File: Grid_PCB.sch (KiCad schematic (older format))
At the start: 1 part, among them U1 74LS151

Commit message: transered nested project into root and moved docs into docs/ folder
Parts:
- removed U1: 74LS151, symbol 74xx:74LS151
- added J10: LED_Conn, Connector_PinHeader_2.54mm:PinHeader_1x02_P2.54mm_Horizontal, symbol Connector:Conn_01x02_Male
- added J9: ESP_Conn, Connector_PinHeader_2.54mm:PinHeader_1x08_P2.54mm_Horizontal, symbol grid:ESP_Conn
- added U1: SN74HC151N, Package_DIP:DIP-16_W7.62mm, symbol grid:SN74HC151N
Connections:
- net labels added: BTN1, BTN2, BTN3, BTN4, BTN5, BTN6, BTN7, ESPselA, ESPselB, ESPselC, LED_In, LED_Link, LED_Out, MUX_OUT
- net labels removed: LED_Serial
- wire segments 4 -> 43
- no-connect marks 0 -> 2
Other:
- note added: "Note the order of these can be changed for ease of routing\njust needs to match up with esp connector (or not, we could just change\norientations/ordering in the cables)"
- note added: "TODO: DO WE WANT TO CONNECT STROBE TO TEST PAD FOR DEBUGGING?"
- note added: "Y = output\nW = inverted output\nG = inverted strobe"
- note removed: "NOTE: we are using the 74HC151 \n(from the shop) but this has \nidentical pinout"

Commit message: temp
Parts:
- U1: footprint Package_DIP:DIP-16_W7.62mm -> Battery:BatteryHolder_Keystone_3000_1x12mm
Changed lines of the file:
@@
 F 0 "U1" H 3250 5225 50  0000 C CNN
 F 1 "SN74HC151N" H 3250 5134 50  0000 C CNN
-F 2 "Package_DIP:DIP-16_W7.62mm" H 3300 4650 50  0001 C CNN
+F 2 "Battery:BatteryHolder_Keystone_3000_1x12mm" H 3300 4650 50  0001 C CNN
 F 3 "https://www.ti.com/lit/ds/symlink/sn74hc151.pdf?ts=1632846774937&ref_url=https%253A%252F%252Fwww.google.com%252F" H 3300 4650 50  0001 C CNN
 	1    3250 4650

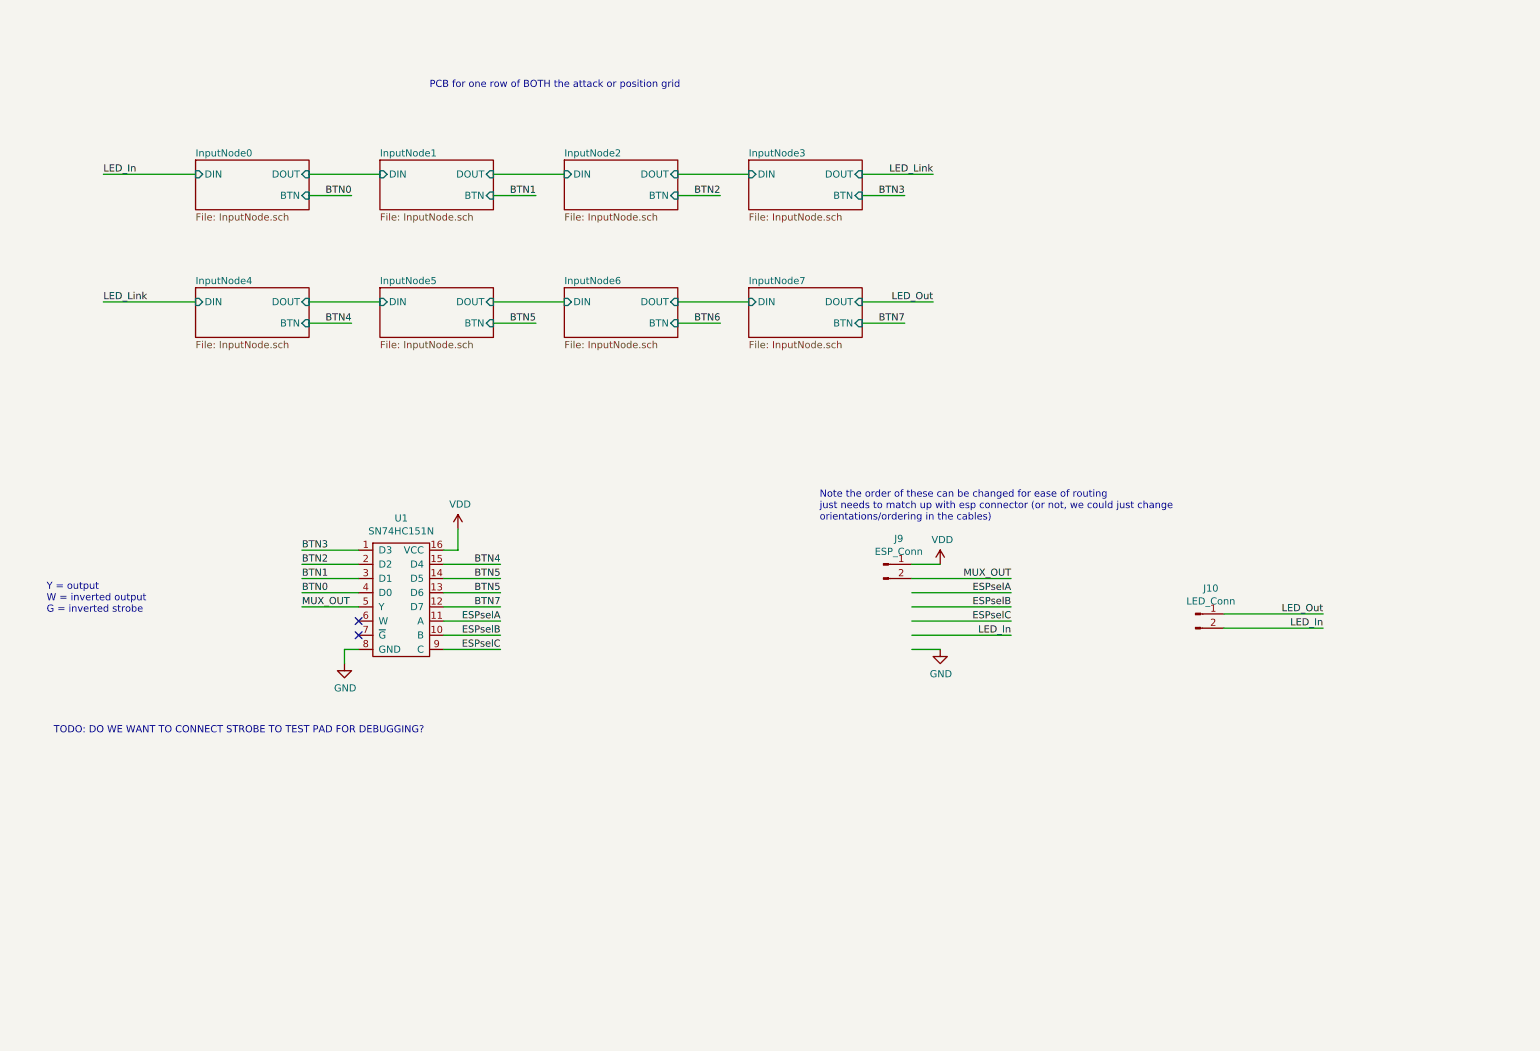
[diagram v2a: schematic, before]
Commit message: updated for homepage
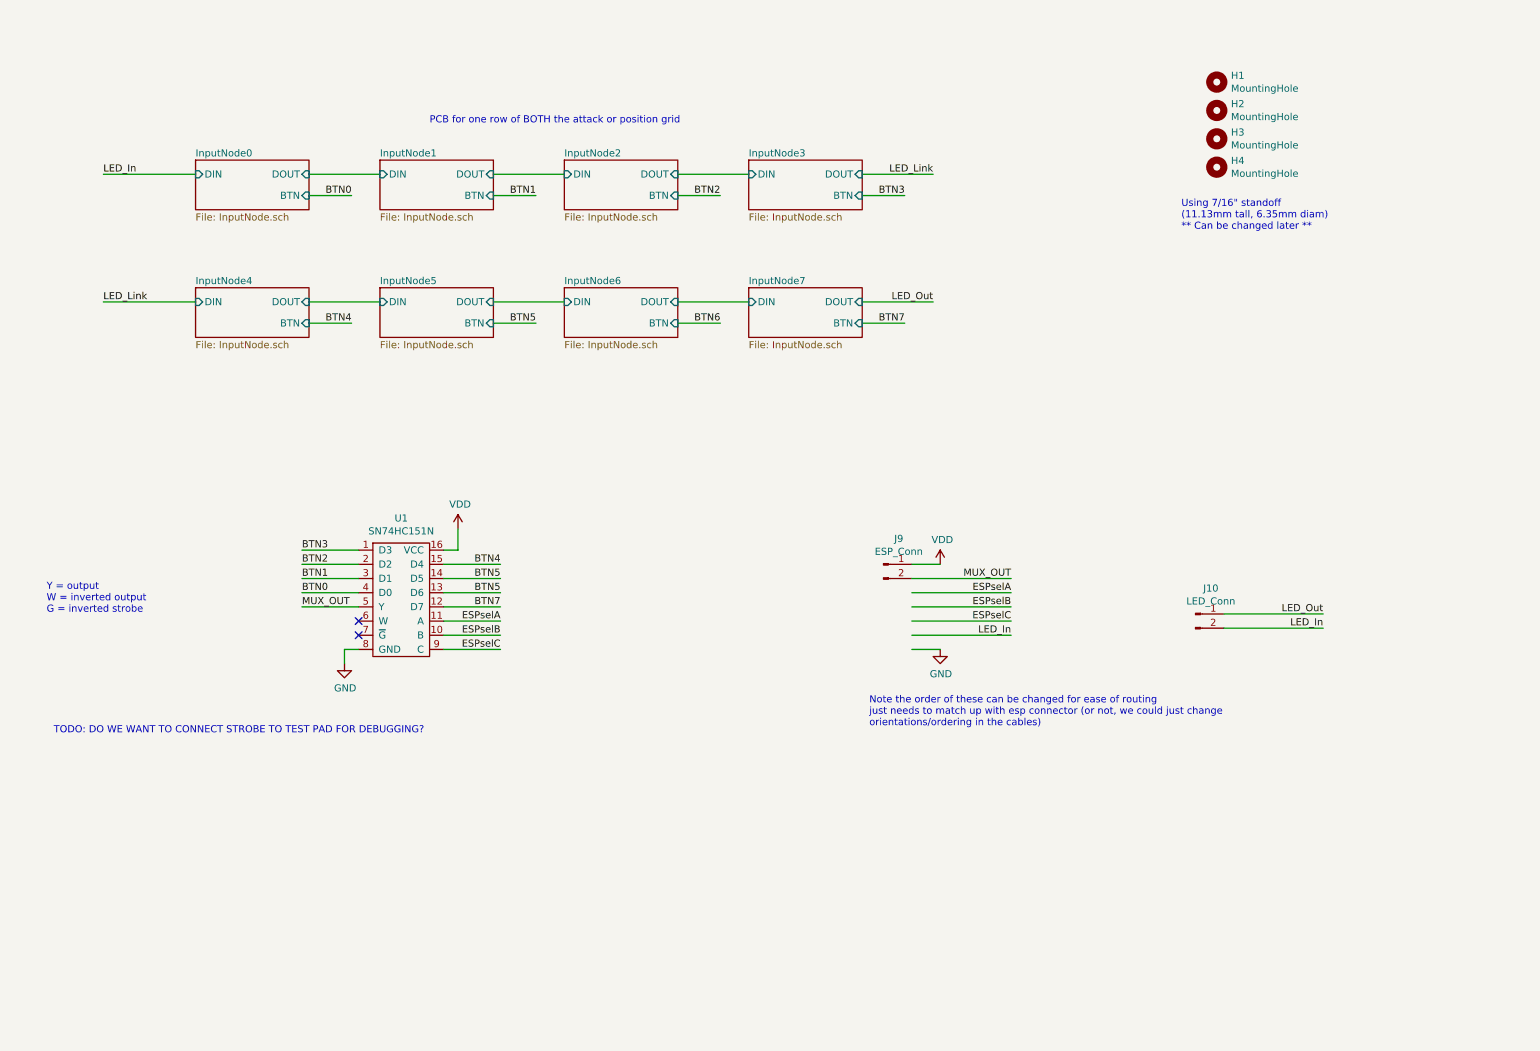
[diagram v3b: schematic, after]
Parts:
- added H1, H2, H3, H4: MountingHole, MountingHole:MountingHole_6.4mm_M6, symbol Mechanical:MountingHole
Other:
- note added: "Using 7/16" standoff \n(11.13mm tall, 6.35mm diam)\n** Can be changed later **"
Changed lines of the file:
@@
 Text Label 6800 2700 2    50   ~ 0
 BTN7
-Text Notes 3450 1050 0    50   ~ 0
+Text Notes 3450 1300 0    50   ~ 0
 PCB for one row of BOTH the attack or position grid
 Wire Wire Line
@@
 Text Label 7550 4500 2    50   ~ 0
 MUX_OUT
-Text Notes 6200 4100 0    50   ~ 0
+Text Notes 6550 5550 0    50   ~ 0
 Note the order of these can be changed for ease of routing\njust needs to match up with esp connector (or not, we could just change\norientations/ordering in the cables)
 Text Label 7550 4600 2    50   ~ 0
@@
 	1    0    0    -1
 $EndComp
+$Comp
+L Mechanical:MountingHole H1
+U 1 1 61A94890
+P 9000 1000
+F 0 "H1" H 9100 1046 50  0000 L CNN
+F 1 "MountingHole" H 9100 955 50  0000 L CNN
+F 2 "MountingHole:MountingHole_6.4mm_M6" H 9000 1000 50  0001 C CNN
+F 3 "~" H 9000 1000 50  0001 C CNN
+	1    9000 1000
+	1    0    0    -1
+$EndComp
+$Comp
+L Mechanical:MountingHole H2
+U 1 1 61A94CB6
+P 9000 1200
+F 0 "H2" H 9100 1246 50  0000 L CNN
+F 1 "MountingHole" H 9100 1155 50  0000 L CNN
+F 2 "MountingHole:MountingHole_6.4mm_M6" H 9000 1200 50  0001 C CNN
+F 3 "~" H 9000 1200 50  0001 C CNN
+	1    9000 1200
+	1    0    0    -1
+$EndComp
+$Comp
+L Mechanical:MountingHole H3
+U 1 1 61A94DFE
+P 9000 1400
+F 0 "H3" H 9100 1446 50  0000 L CNN
+F 1 "MountingHole" H 9100 1355 50  0000 L CNN
+F 2 "MountingHole:MountingHole_6.4mm_M6" H 9000 1400 50  0001 C CNN
+F 3 "~" H 9000 1400 50  0001 C CNN
+	1    9000 1400
+	1    0    0    -1
+$EndComp
+$Comp
+L Mechanical:MountingHole H4
+U 1 1 61A94FF8
+P 9000 1600
+F 0 "H4" H 9100 1646 50  0000 L CNN
+F 1 "MountingHole" H 9100 1555 50  0000 L CNN
+F 2 "MountingHole:MountingHole_6.4mm_M6" H 9000 1600 50  0001 C CNN
+F 3 "~" H 9000 1600 50  0001 C CNN
+	1    9000 1600
+	1    0    0    -1
+$EndComp
+Text Notes 8750 2050 0    50   ~ 0
+Using 7/16" standoff \n(11.13mm tall, 6.35mm diam)\n** Can be changed later **
 $EndSCHEMATC

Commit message: added resistor network and updated mnt hole footprint
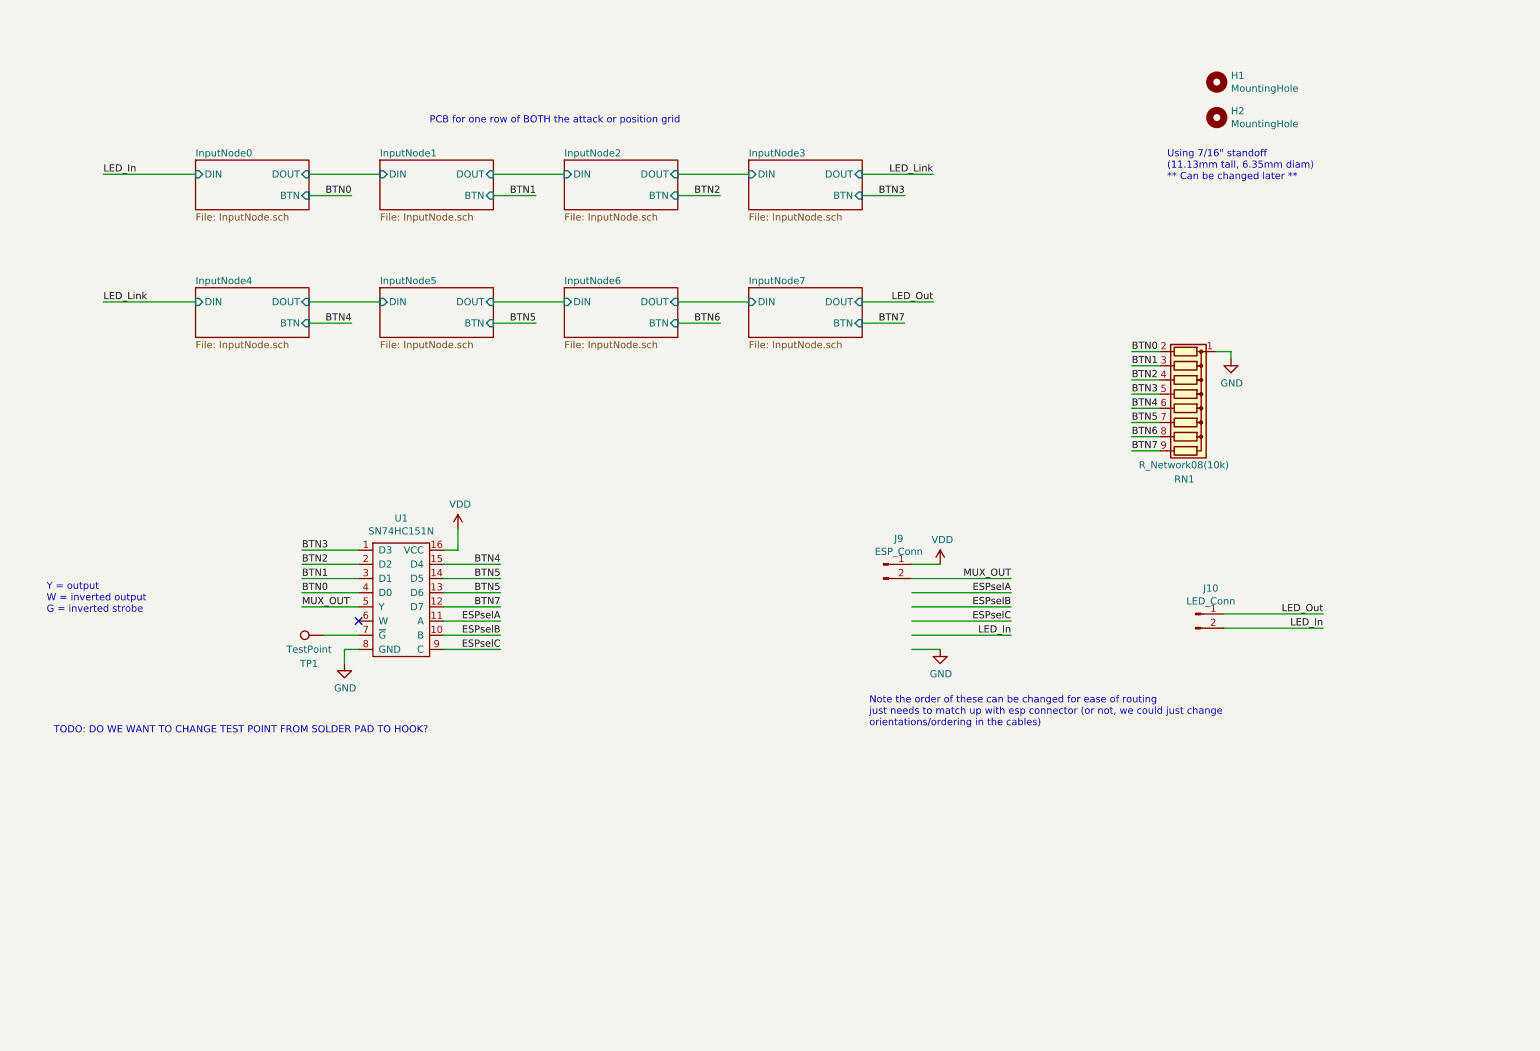
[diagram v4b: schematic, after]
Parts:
- removed H3, H4: MountingHole, MountingHole:MountingHole_6.4mm_M6, symbol Mechanical:MountingHole
- added RN1: R_Network08(10k), Resistor_THT:R_Array_SIP9, symbol Device:R_Network08
- added TP1: TestPoint, TestPoint:TestPoint_Pad_2.5x2.5mm, symbol Connector:TestPoint
- H1, H2: footprint MountingHole:MountingHole_6.4mm_M6 -> MountingHole:MountingHole_3.2mm_M3
- U1: footprint Battery:BatteryHolder_Keystone_3000_1x12mm -> Package_DIP:DIP-16_W10.16mm
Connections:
- wire segments 43 -> 54
- no-connect marks 2 -> 1
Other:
- note added: "TODO: DO WE WANT TO CHANGE TEST POINT FROM SOLDER PAD TO HOOK?"
- note removed: "TODO: DO WE WANT TO CONNECT STROBE TO TEST PAD FOR DEBUGGING?"
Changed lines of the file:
@@
 F 0 "U1" H 3250 5225 50  0000 C CNN
 F 1 "SN74HC151N" H 3250 5134 50  0000 C CNN
-F 2 "Battery:BatteryHolder_Keystone_3000_1x12mm" H 3300 4650 50  0001 C CNN
+F 2 "Package_DIP:DIP-16_W10.16mm" H 3300 4650 50  0001 C CNN
 F 3 "https://www.ti.com/lit/ds/symlink/sn74hc151.pdf?ts=1632846774937&ref_url=https%253A%252F%252Fwww.google.com%252F" H 3300 4650 50  0001 C CNN
 	1    3250 4650
@@
 Wire Wire Line
 	6850 4500 7550 4500
-NoConn ~ 2950 4900
 Text Notes 800  5600 0    50   ~ 0
-TODO: DO WE WANT TO CONNECT STROBE TO TEST PAD FOR DEBUGGING?
+TODO: DO WE WANT TO CHANGE TEST POINT FROM SOLDER PAD TO HOOK?
 NoConn ~ 2950 4800
 Text Label 2550 4700 0    50   ~ 0
@@
 F 0 "H1" H 9100 1046 50  0000 L CNN
 F 1 "MountingHole" H 9100 955 50  0000 L CNN
-F 2 "MountingHole:MountingHole_6.4mm_M6" H 9000 1000 50  0001 C CNN
-F 3 "~" H 9000 1000 50  0001 C CNN
+F 2 "MountingHole:MountingHole_3.2mm_M3" H 9000 1000 50  0001 C CNN
+F 3 "https://www.digikey.com/en/products/detail/essentra-components/50M030050F012/11639328~" H 9000 1000 50  0001 C CNN
 	1    9000 1000
 	1    0    0    -1
 $EndComp
+Text Notes 8650 1700 0    50   ~ 0
+Using 7/16" standoff \n(11.13mm tall, 6.35mm diam)\n** Can be changed later **
+$Comp
+L Connector:TestPoint TP1
+U 1 1 615B44CF
+P 2700 4900
+F 0 "TP1" V 2500 5000 50  0000 C CNN
+F 1 "TestPoint" V 2600 5000 50  0000 C CNN
+F 2 "TestPoint:TestPoint_Pad_2.5x2.5mm" H 2900 4900 50  0001 C CNN
+F 3 "~" H 2900 4900 50  0001 C CNN
+	1    2700 4900
+	0    -1   -1   0
+$EndComp
+Wire Wire Line
+	2700 4900 2950 4900
+$Comp
+L Device:R_Network08 RN1
+U 1 1 615B83C9
+P 8800 3300
+F 0 "RN1" V 9300 3200 50  0000 L CNN
+F 1 "R_Network08(10k)" V 9200 2950 50  0000 L CNN
+F 2 "Resistor_THT:R_Array_SIP9" V 9275 3300 50  0001 C CNN
+F 3 "http://www.vishay.com/docs/31509/csc.pdf" H 8800 3300 50  0001 C CNN
+	1    8800 3300
+	0    1    1    0
+$EndComp
+$Comp
+L power:GND #PWR051
+U 1 1 615BC30E
+P 9100 2950
+F 0 "#PWR051" H 9100 2700 50  0001 C CNN
+F 1 "GND" H 9105 2777 50  0000 C CNN
+F 2 "" H 9100 2950 50  0001 C CNN
+F 3 "" H 9100 2950 50  0001 C CNN
+	1    9100 2950
+	1    0    0    -1
+$EndComp
+Text Label 8400 2900 0    50   ~ 0
+BTN0
+Wire Wire Line
+	8400 2900 8600 2900
+Text Label 8400 3000 0    50   ~ 0
+BTN1
+Wire Wire Line
+	8400 3000 8600 3000
+Text Label 8400 3100 0    50   ~ 0
+BTN2
+Wire Wire Line
+	8400 3100 8600 3100
+Text Label 8400 3200 0    50   ~ 0
+BTN3
+Wire Wire Line
+	8400 3200 8600 3200
+Text Label 8400 3300 0    50   ~ 0
+BTN4
+Wire Wire Line
+	8400 3300 8600 3300
+Text Label 8400 3400 0    50   ~ 0
+BTN5
+Wire Wire Line
+	8400 3400 8600 3400
+Text Label 8400 3500 0    50   ~ 0
+BTN6
+Wire Wire Line
+	8400 3500 8600 3500
+Text Label 8400 3600 0    50   ~ 0
+BTN7
+Wire Wire Line
+	8400 3600 8600 3600
+Wire Wire Line
+	9000 2900 9100 2900
+Wire Wire Line
+	9100 2900 9100 2950
 $Comp
 L Mechanical:MountingHole H2
-U 1 1 61A94CB6
-P 9000 1200
-F 0 "H2" H 9100 1246 50  0000 L CNN
-F 1 "MountingHole" H 9100 1155 50  0000 L CNN
-F 2 "MountingHole:MountingHole_6.4mm_M6" H 9000 1200 50  0001 C CNN
-F 3 "~" H 9000 1200 50  0001 C CNN
-	1    9000 1200
-	1    0    0    -1
-$EndComp
-$Comp
-L Mechanical:MountingHole H3
-U 1 1 61A94DFE
-P 9000 1400
-F 0 "H3" H 9100 1446 50  0000 L CNN
-F 1 "MountingHole" H 9100 1355 50  0000 L CNN
-F 2 "MountingHole:MountingHole_6.4mm_M6" H 9000 1400 50  0001 C CNN
-F 3 "~" H 9000 1400 50  0001 C CNN
-	1    9000 1400
-	1    0    0    -1
-$EndComp
-$Comp
-L Mechanical:MountingHole H4
-U 1 1 61A94FF8
-P 9000 1600
-F 0 "H4" H 9100 1646 50  0000 L CNN
-F 1 "MountingHole" H 9100 1555 50  0000 L CNN
-F 2 "MountingHole:MountingHole_6.4mm_M6" H 9000 1600 50  0001 C CNN
-F 3 "~" H 9000 1600 50  0001 C CNN
-	1    9000 1600
-	1    0    0    -1
-$EndComp
-Text Notes 8750 2050 0    50   ~ 0
-Using 7/16" standoff \n(11.13mm tall, 6.35mm diam)\n** Can be changed later **
+U 1 1 615D2E17
+P 9000 1250
+F 0 "H2" H 9100 1296 50  0000 L CNN
+F 1 "MountingHole" H 9100 1205 50  0000 L CNN
+F 2 "MountingHole:MountingHole_3.2mm_M3" H 9000 1250 50  0001 C CNN
+F 3 "https://www.digikey.com/en/products/detail/essentra-components/50M030050F012/11639328~" H 9000 1250 50  0001 C CNN
+	1    9000 1250
+	1    0    0    -1
+$EndComp
 $EndSCHEMATC

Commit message: finished first pass at routing
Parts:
- removed RN1: R_Network08(10k), Resistor_THT:R_Array_SIP9, symbol Device:R_Network08
- added H3, H4: MountingHole, MountingHole:MountingHole_3.2mm_M3, symbol Mechanical:MountingHole
- J9: footprint Connector_PinHeader_2.54mm:PinHeader_1x08_P2.54mm_Horizontal -> Connector_PinHeader_2.54mm:PinHeader_1x07_P2.54mm_Horizontal
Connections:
- wire segments 54 -> 44
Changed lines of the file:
@@
 	3950 4500 3550 4500
 Text Label 3950 4600 2    50   ~ 0
-BTN5
+BTN6
 Wire Wire Line
 	3950 4600 3550 4600
@@
 PCB for one row of BOTH the attack or position grid
 Wire Wire Line
-	6850 4500 7550 4500
+	6850 4800 7550 4800
 Text Notes 800  5600 0    50   ~ 0
 TODO: DO WE WANT TO CHANGE TEST POINT FROM SOLDER PAD TO HOOK?
@@
 Wire Wire Line
 	2550 4700 2950 4700
-Text Label 7550 4500 2    50   ~ 0
+Text Label 7550 4800 2    50   ~ 0
 MUX_OUT
 Text Notes 6550 5550 0    50   ~ 0
 Note the order of these can be changed for ease of routing\njust needs to match up with esp connector (or not, we could just change\norientations/ordering in the cables)
+Text Label 7550 4700 2    50   ~ 0
+ESPselA
+Text Label 7550 4500 2    50   ~ 0
+ESPselC
 Text Label 7550 4600 2    50   ~ 0
-ESPselA
-Text Label 7550 4800 2    50   ~ 0
-ESPselC
-Text Label 7550 4700 2    50   ~ 0
 ESPselB
 Wire Wire Line
-	6850 4600 7550 4600
-Wire Wire Line
-	7550 4700 6850 4700
-Wire Wire Line
-	6850 4800 7550 4800
+	6850 4500 7550 4500
+Wire Wire Line
+	7550 4600 6850 4600
+Wire Wire Line
+	6850 4700 7550 4700
 Text Label 7550 4900 2    50   ~ 0
 LED_In
@@
 Wire Wire Line
 	9050 4750 9750 4750
+Text Label 9750 4750 2    50   ~ 0
+LED_In
+Wire Wire Line
+	9050 4850 9750 4850
 Text Label 9750 4850 2    50   ~ 0
-LED_In
-Wire Wire Line
-	9050 4850 9750 4850
-Text Label 9750 4750 2    50   ~ 0
 LED_Out
 Wire Wire Line
@@
 F 0 "J9" H 6758 5181 50  0000 C CNN
 F 1 "ESP_Conn" H 6758 5090 50  0000 C CNN
-F 2 "Connector_PinHeader_2.54mm:PinHeader_1x08_P2.54mm_Horizontal" H 6650 4700 50  0001 C CNN
+F 2 "Connector_PinHeader_2.54mm:PinHeader_1x07_P2.54mm_Horizontal" H 6650 4700 50  0001 C CNN
 F 3 "~" H 6650 4700 50  0001 C CNN
 	1    6650 4700
@@
 	2700 4900 2950 4900
 $Comp
-L Device:R_Network08 RN1
-U 1 1 615B83C9
-P 8800 3300
-F 0 "RN1" V 9300 3200 50  0000 L CNN
-F 1 "R_Network08(10k)" V 9200 2950 50  0000 L CNN
-F 2 "Resistor_THT:R_Array_SIP9" V 9275 3300 50  0001 C CNN
-F 3 "http://www.vishay.com/docs/31509/csc.pdf" H 8800 3300 50  0001 C CNN
-	1    8800 3300
-	0    1    1    0
-$EndComp
-$Comp
-L power:GND #PWR051
-U 1 1 615BC30E
-P 9100 2950
-F 0 "#PWR051" H 9100 2700 50  0001 C CNN
-F 1 "GND" H 9105 2777 50  0000 C CNN
-F 2 "" H 9100 2950 50  0001 C CNN
-F 3 "" H 9100 2950 50  0001 C CNN
-	1    9100 2950
-	1    0    0    -1
-$EndComp
-Text Label 8400 2900 0    50   ~ 0
-BTN0
-Wire Wire Line
-	8400 2900 8600 2900
-Text Label 8400 3000 0    50   ~ 0
-BTN1
-Wire Wire Line
-	8400 3000 8600 3000
-Text Label 8400 3100 0    50   ~ 0
-BTN2
-Wire Wire Line
-	8400 3100 8600 3100
-Text Label 8400 3200 0    50   ~ 0
-BTN3
-Wire Wire Line
-	8400 3200 8600 3200
-Text Label 8400 3300 0    50   ~ 0
-BTN4
-Wire Wire Line
-	8400 3300 8600 3300
-Text Label 8400 3400 0    50   ~ 0
-BTN5
-Wire Wire Line
-	8400 3400 8600 3400
-Text Label 8400 3500 0    50   ~ 0
-BTN6
-Wire Wire Line
-	8400 3500 8600 3500
-Text Label 8400 3600 0    50   ~ 0
-BTN7
-Wire Wire Line
-	8400 3600 8600 3600
-Wire Wire Line
-	9000 2900 9100 2900
-Wire Wire Line
-	9100 2900 9100 2950
-$Comp
 L Mechanical:MountingHole H2
 U 1 1 615D2E17
@@
 	1    0    0    -1
 $EndComp
+$Comp
+L Mechanical:MountingHole H3
+U 1 1 615EB804
+P 9800 1000
+F 0 "H3" H 9900 1046 50  0000 L CNN
+F 1 "MountingHole" H 9900 955 50  0000 L CNN
+F 2 "MountingHole:MountingHole_3.2mm_M3" H 9800 1000 50  0001 C CNN
+F 3 "https://www.digikey.com/en/products/detail/essentra-components/50M030050F012/11639328~" H 9800 1000 50  0001 C CNN
+	1    9800 1000
+	1    0    0    -1
+$EndComp
+$Comp
+L Mechanical:MountingHole H4
+U 1 1 615EB80A
+P 9800 1250
+F 0 "H4" H 9900 1296 50  0000 L CNN
+F 1 "MountingHole" H 9900 1205 50  0000 L CNN
+F 2 "MountingHole:MountingHole_3.2mm_M3" H 9800 1250 50  0001 C CNN
+F 3 "https://www.digikey.com/en/products/detail/essentra-components/50M030050F012/11639328~" H 9800 1250 50  0001 C CNN
+	1    9800 1250
+	1    0    0    -1
+$EndComp
